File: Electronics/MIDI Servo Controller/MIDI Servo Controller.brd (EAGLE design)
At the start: 59 x 66 mm, 26 parts, among them Q1 20MHz, T1 2N3904, X1 SIGNAL-PWR-GND, X2 SIGNAL-PWR-GND

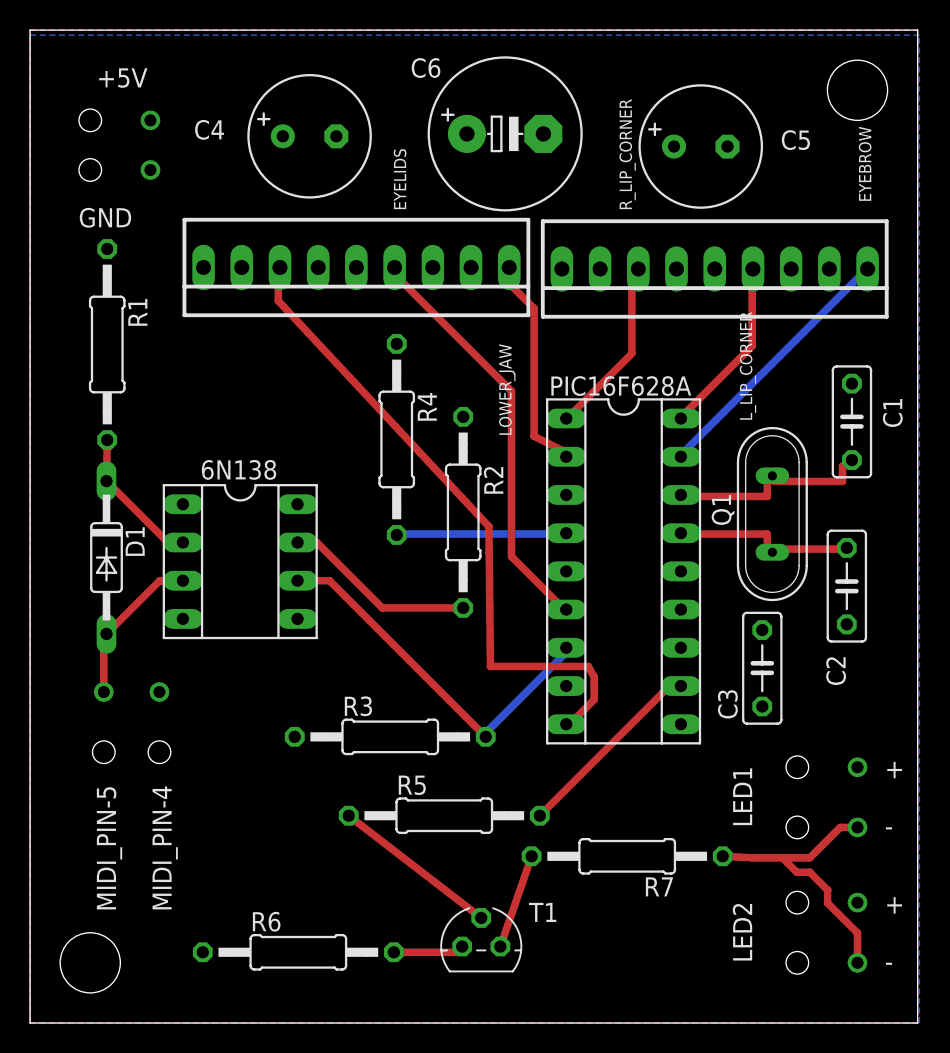
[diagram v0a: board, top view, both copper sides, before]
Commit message: Cleaned up schematic and board layout.
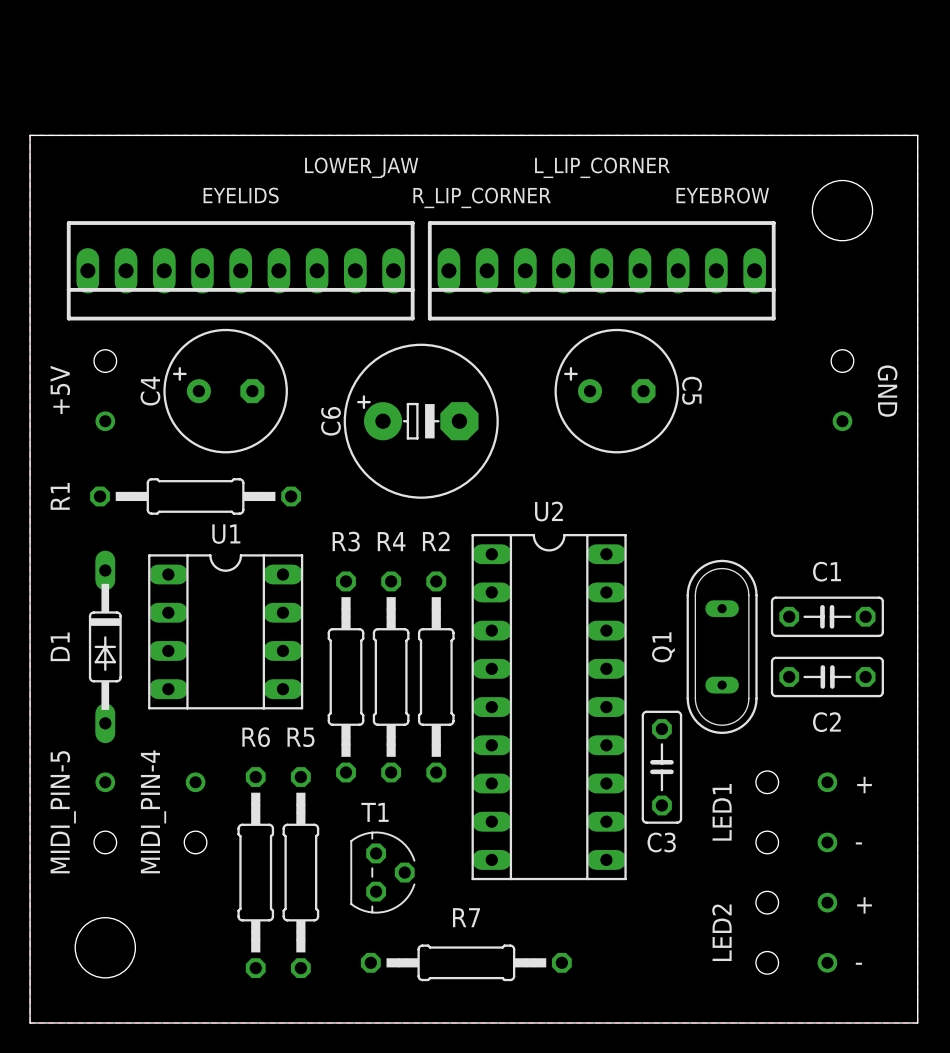
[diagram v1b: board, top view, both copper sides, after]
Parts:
- 6N138: value (none) -> U1
- PIC16F628A: value (none) -> U2
- moved GND 50.2 mm to (54.0, 42.0), turned to 90 degrees
- moved C6 19.9 mm to (26.0, 40.0)
- moved +5V 18.0 mm to (5.00, 42.0), turned to 90 degrees
- moved C4 17.8 mm to (13.0, 42.0)
- moved C5 17.2 mm to (39.0, 42.0)
- moved R4 15.8 mm to (24.0, 23.0)
- moved C1 13.1 mm to (53.0, 27.0), turned to 180 degrees
- moved R7 12.8 mm to (29.0, 4.00)
- moved R1 11.7 mm to (11.0, 35.0), turned to 180 degrees
- moved R2 11.1 mm to (27.0, 23.0)
- moved PIC16F628A 10.3 mm to (34.5, 21.0)
- moved R5 10.3 mm to (18.0, 10.0), turned to 90 degrees
- moved Q1 9.44 mm to (46.0, 25.0)
- moved C3 9.37 mm to (42.0, 17.0)
- moved T1 8.55 mm to (23.0, 10.0), turned to 270 degrees
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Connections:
- net N$3 renamed OSC1
- net N$4 renamed OSC2
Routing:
- net UNUSED: track 43.4 -> 0.00 mm
- net EYELIDS: track 27.5 -> 0.00 mm
- net RX_PIN: track 24.9 -> 0.00 mm
- net N$10: track 19.4 -> 0.00 mm
- net EYEBROW: track 17.6 -> 0.00 mm
- net LOWER_JAR: track 14.5 -> 0.00 mm
- net OSC1: track 13.9 -> 0.00 mm
- net LIGHTS: track 13.0 -> 0.00 mm
- net N$2: track 12.8 -> 0.00 mm
- net OSC2: track 12.2 -> 0.00 mm
- net RIGHT_LIP_CORNER: track 12.1 -> 0.00 mm
- net LEFT_LIP_CORNER: track 11.9 -> 0.00 mm
- net N$6: track 11.3 -> 0.00 mm
- net N$5: track 11.1 -> 0.00 mm
- net MIDI_PIN-5: track 10.5 -> 0.00 mm
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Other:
- board size 59 x 66 mm -> 59 x 59 mm

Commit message: Updated schematic and board layout with updated component library.
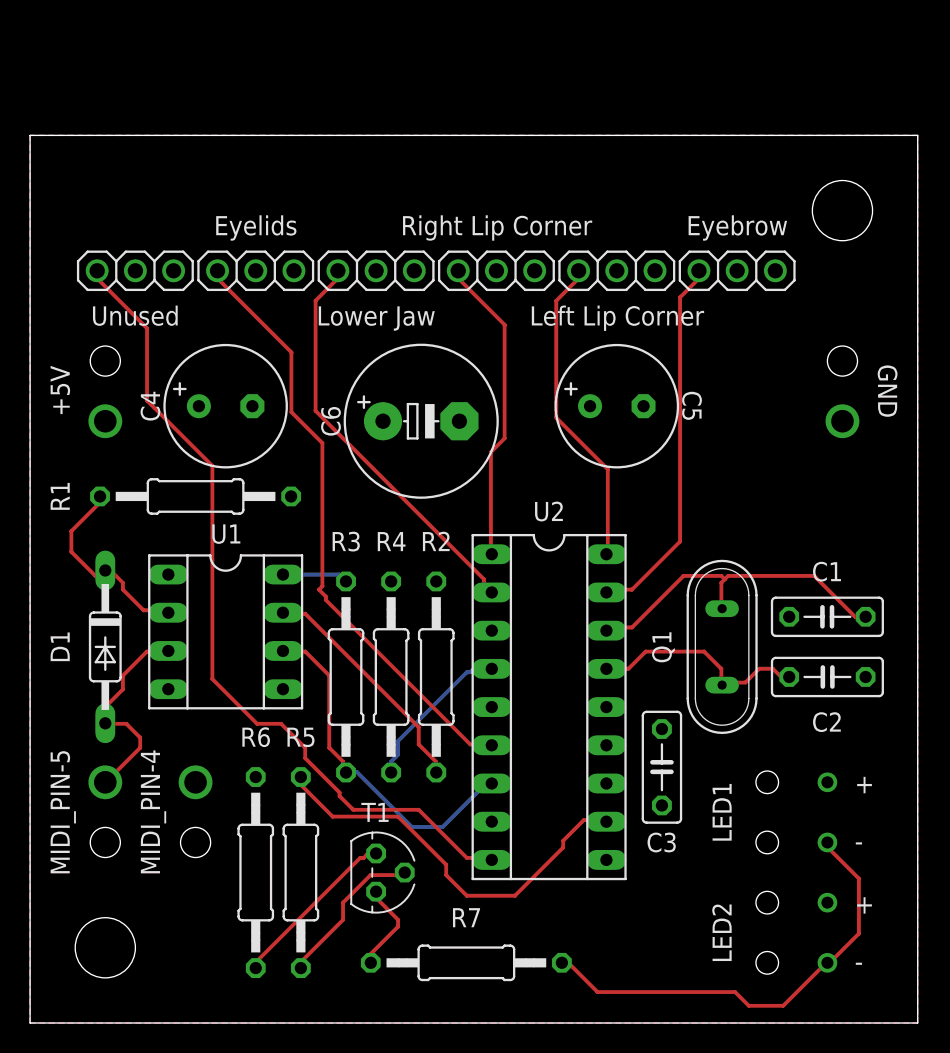
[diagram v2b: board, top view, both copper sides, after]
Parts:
- removed X1, X2: SIGNAL-PWR-GND, con-molex:22-23-2091
- added JP1: Eyebrow, adafruit:1X03
- added JP2: Left Lip Corner, adafruit:1X03
- added JP3: Right Lip Corner, adafruit:1X03
- added JP4: Lower Jaw, adafruit:1X03
- added JP5: Eyelids, adafruit:1X03
- added JP6: Unused, adafruit:1X03
- +5V, GND, MIDI_PIN-4, MIDI_PIN-5: device DOUBLE_THROUGH_HOLE_PAD:DOUBLE_THROUGH_HOLE_PAD -> Double-Through-Hole-Pad:DOUBLE_THROUGH_HOLE_PAD
- LED1, LED2: device REMOTE_LED:REMOTE_LED -> Remote-LED:REMOTE_LED
- moved C4 1.00 mm to (13.0, 41.0)
- moved C5 1.00 mm to (39.0, 41.0)
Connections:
- net +5V: now also JP1.2, JP2.2, JP3.2, JP4.2, JP5.2, JP6.2; no longer X1.2, X1.5, X1.8, X2.2, X2.5, X2.8
- net EYEBROW: now also JP1.1; no longer X2.1
- net EYELIDS: now also JP5.1; no longer X1.4
- net GND: now also JP1.3, JP2.3, JP3.3, JP4.3, JP5.3, JP6.3; no longer X1.3, X1.6, X1.9, X2.3, X2.6, X2.9
- net LEFT_LIP_CORNER: now also JP2.1; no longer X2.4
- net LOWER_JAR: now also JP4.1; no longer X1.1
- net RIGHT_LIP_CORNER: now also JP3.1; no longer X2.7
- net UNUSED: now also JP6.1; no longer X1.7
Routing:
- net UNUSED: track 0.00 -> 54.4 mm
- net EYELIDS: track 0.00 -> 40.1 mm
- net N$10: track 0.00 -> 30.3 mm
- net LOWER_JAR: track 0.00 -> 26.8 mm
- net LIGHTS: track 0.00 -> 26.7 mm
- net EYEBROW: track 0.00 -> 24.8 mm
- net RX_PIN: track 0.00 -> 23.2 mm
- net OSC1: track 0.00 -> 22.2 mm
- net LEFT_LIP_CORNER: track 0.00 -> 20.9 mm
- net RIGHT_LIP_CORNER: track 0.00 -> 20.5 mm
- net N$2: track 0.00 -> 15.7 mm
- net OSC2: track 0.00 -> 14.8 mm
- net MIDI_PIN-5: track 0.00 -> 14.0 mm
- net N$1: track 0.00 -> 13.3 mm
- net N$7: track 0.00 -> 11.4 mm
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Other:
- board text removed: "EYEBROW"
- board text removed: "EYELIDS"
- board text removed: "LOWER_JAW"
- board text removed: "L_LIP_CORNER"
- board text removed: "R_LIP_CORNER"
